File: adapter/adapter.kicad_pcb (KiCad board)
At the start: 2 copper layers, 93.5 x 50.9 mm, 41 parts, among them J10 Ribbon, J11 Ribbon, J12 Ribbon, J9 Ribbon, U1 nice_nano

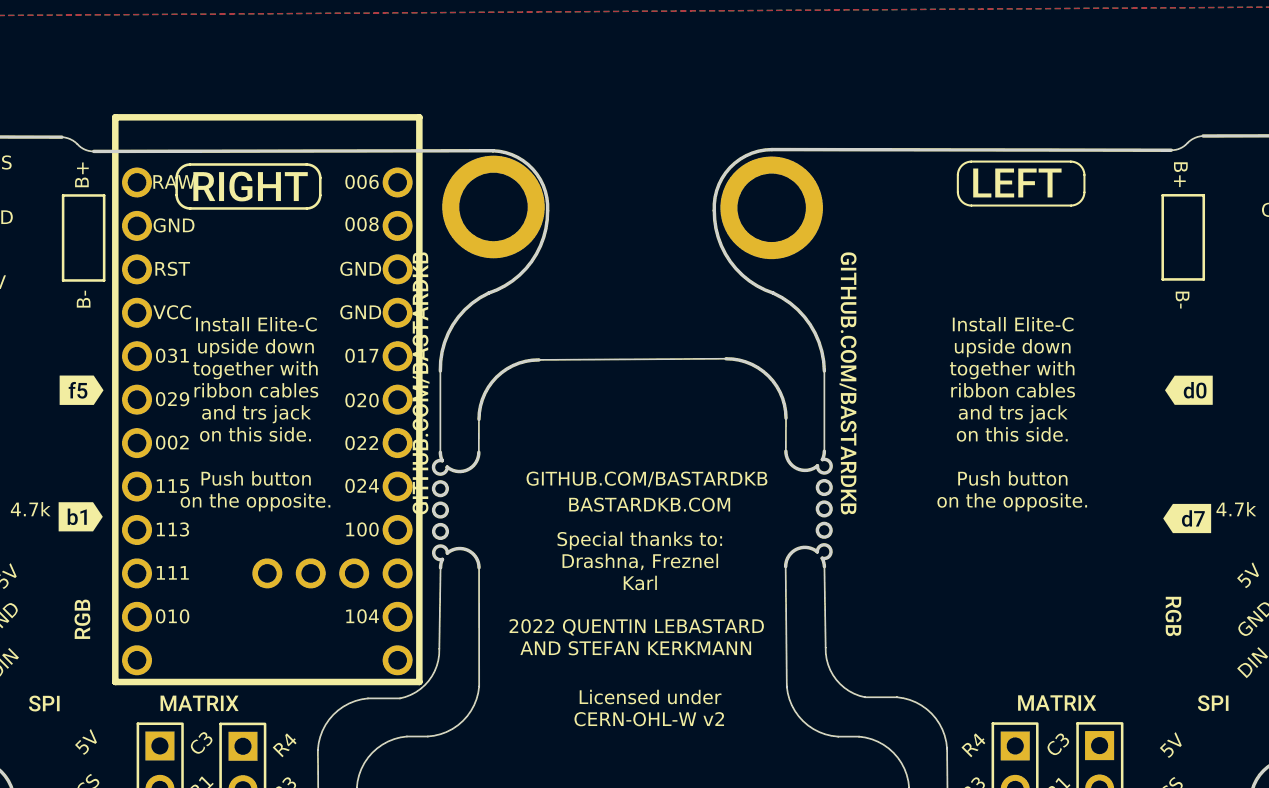
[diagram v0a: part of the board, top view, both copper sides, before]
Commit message: Add nice!nano mcu to right side
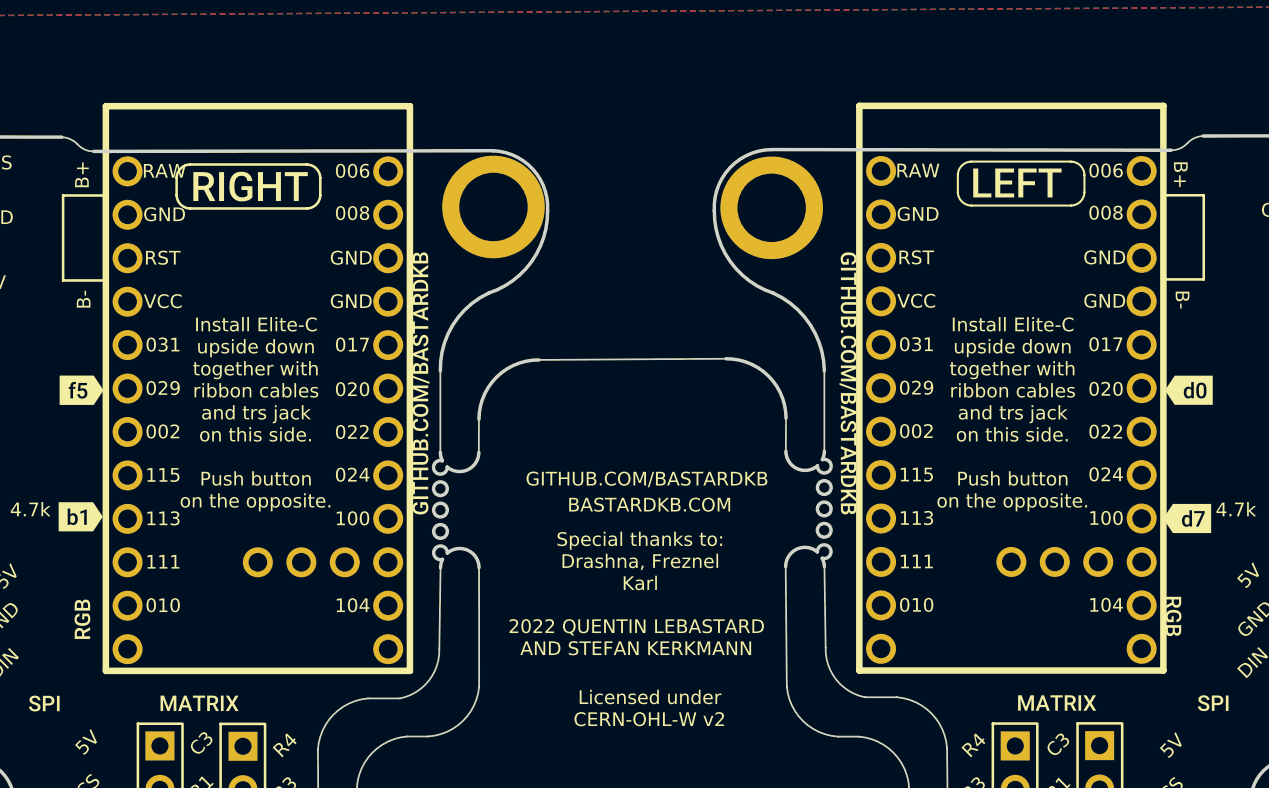
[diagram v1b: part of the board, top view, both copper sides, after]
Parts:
- added U2: nice_nano, Library:nice_nano, B.Cu at (177.6, 83.2)
- moved U1 0.85 mm to (133.6, 83.2)

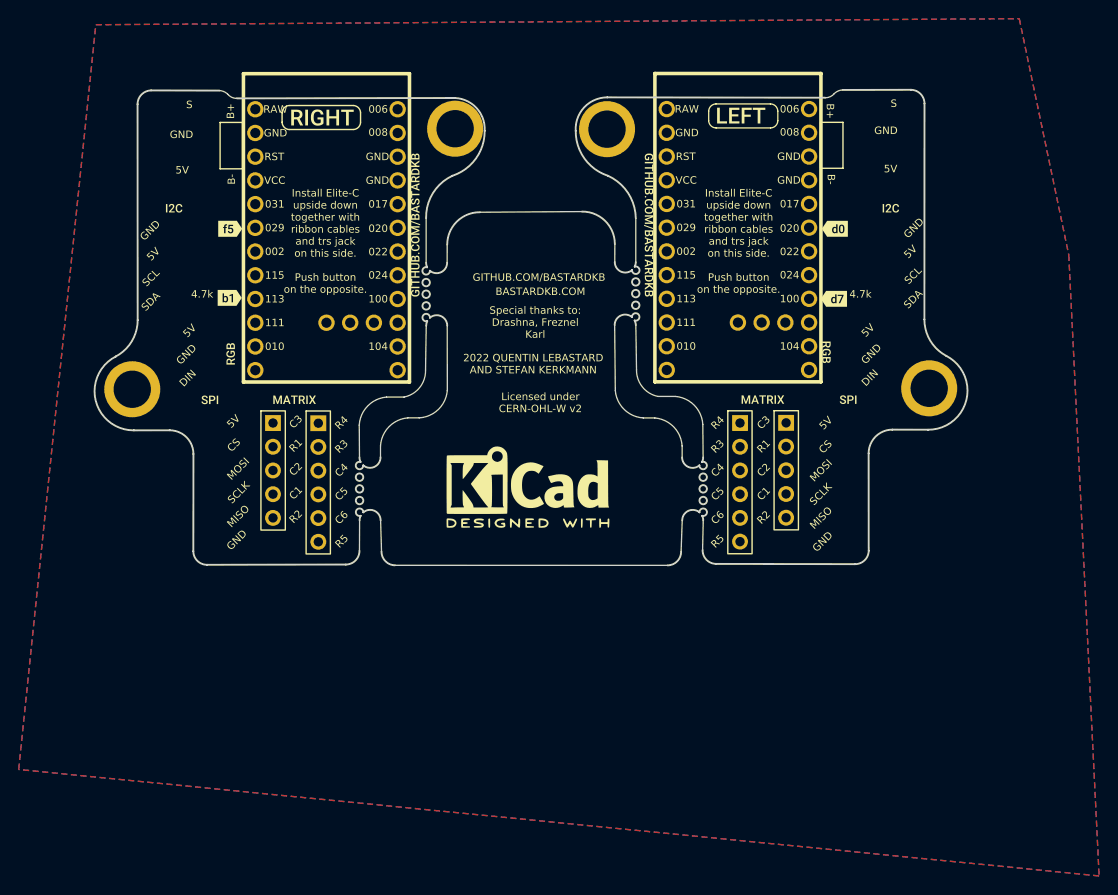
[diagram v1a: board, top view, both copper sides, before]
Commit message: Cleanup all the leftover silkscreen from removed parts
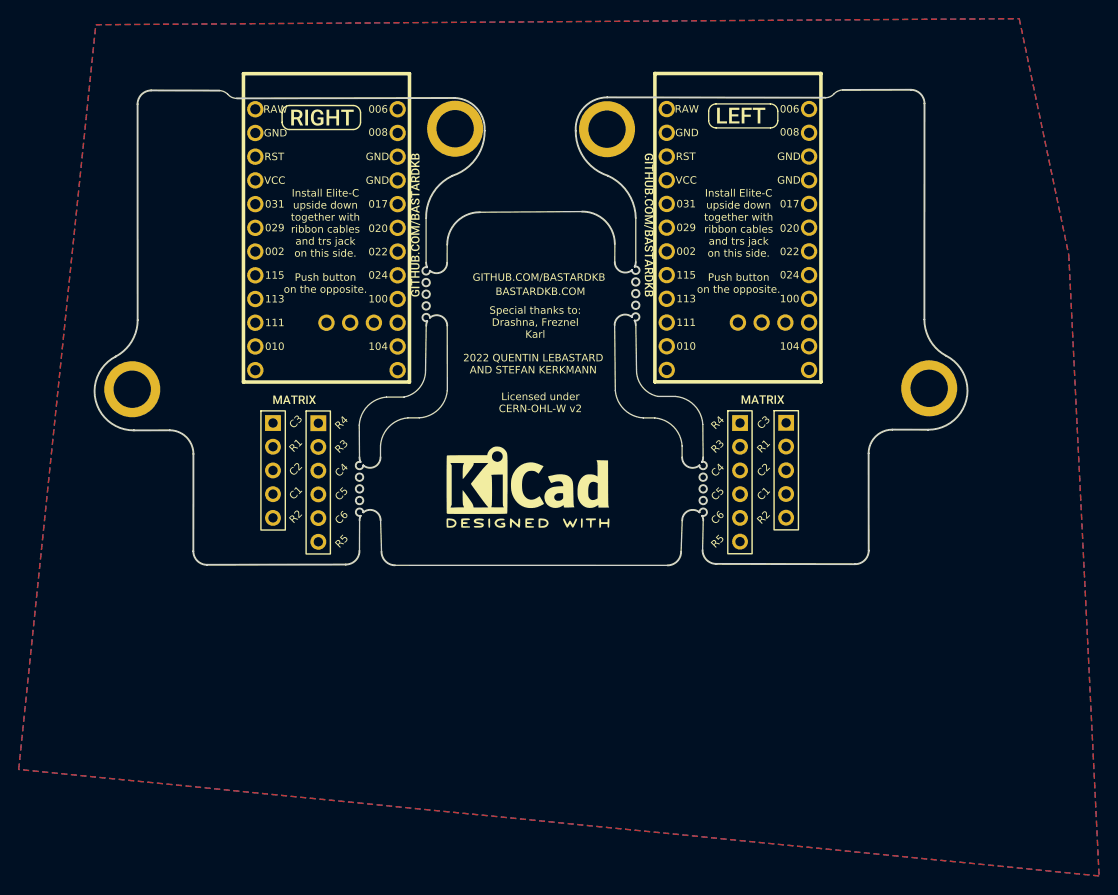
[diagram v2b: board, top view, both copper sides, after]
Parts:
- removed kibuzzard-61F01957 (x4): G***, kibuzzard-61F01957
- removed kibuzzard-61F019CB (x4): G***, kibuzzard-61F019CB
- removed kibuzzard-6208EDFE: G***, kibuzzard-6208EDFE
- removed kibuzzard-6208EE22: G***, kibuzzard-6208EE22
- removed kibuzzard-62093EDE: G***, kibuzzard-62093EDE
- removed kibuzzard-62094D1C: G***, kibuzzard-62094D1C
- removed the kibuzzard-620B8593 at (177.5, 78.6)
- removed kibuzzard-620B8D91 (x4): G***, kibuzzard-620B8D91
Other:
- board text removed: "4.7k"
- board text removed: "5V"
- board text removed: "B+"
- board text removed: "B-"
- board text removed: "CS"
- board text removed: "DIN"
- board text removed: "GND"
- board text removed: "MISO"
- board text removed: "MOSI"
- board text removed: "S"
- board text removed: "SCL"
- board text removed: "SCLK"
- board text removed: "SDA"

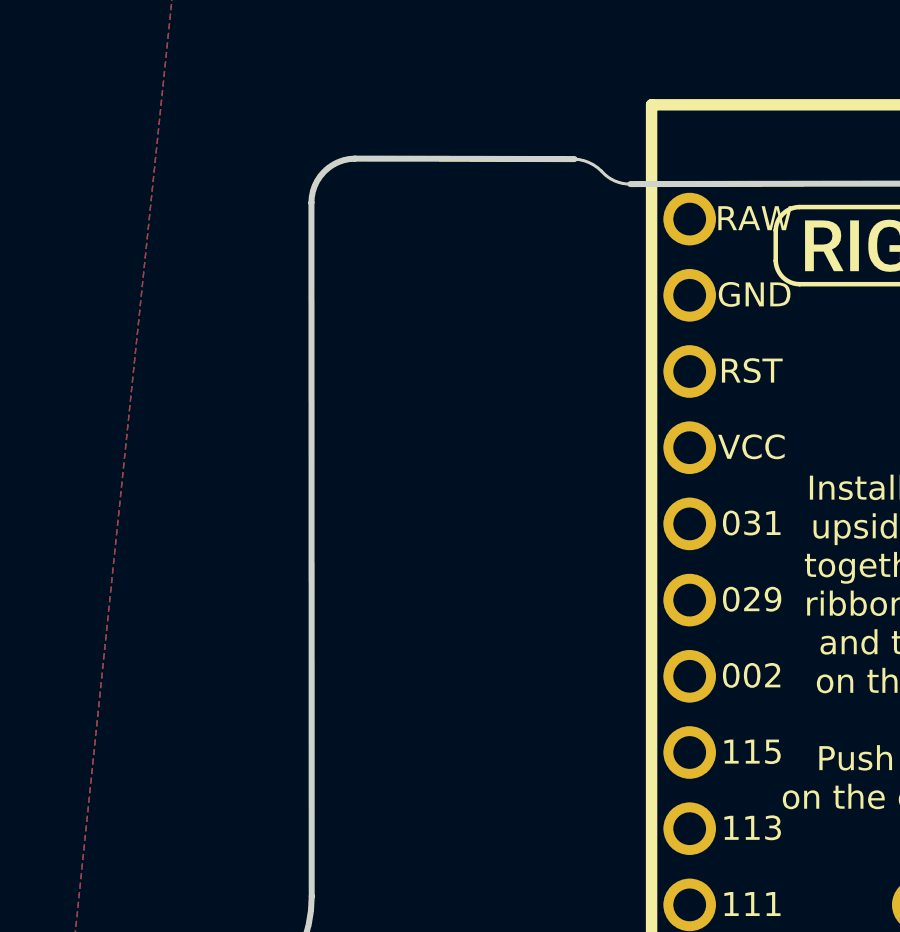
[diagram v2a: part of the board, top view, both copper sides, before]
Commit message: Add jst connector and powerswitch
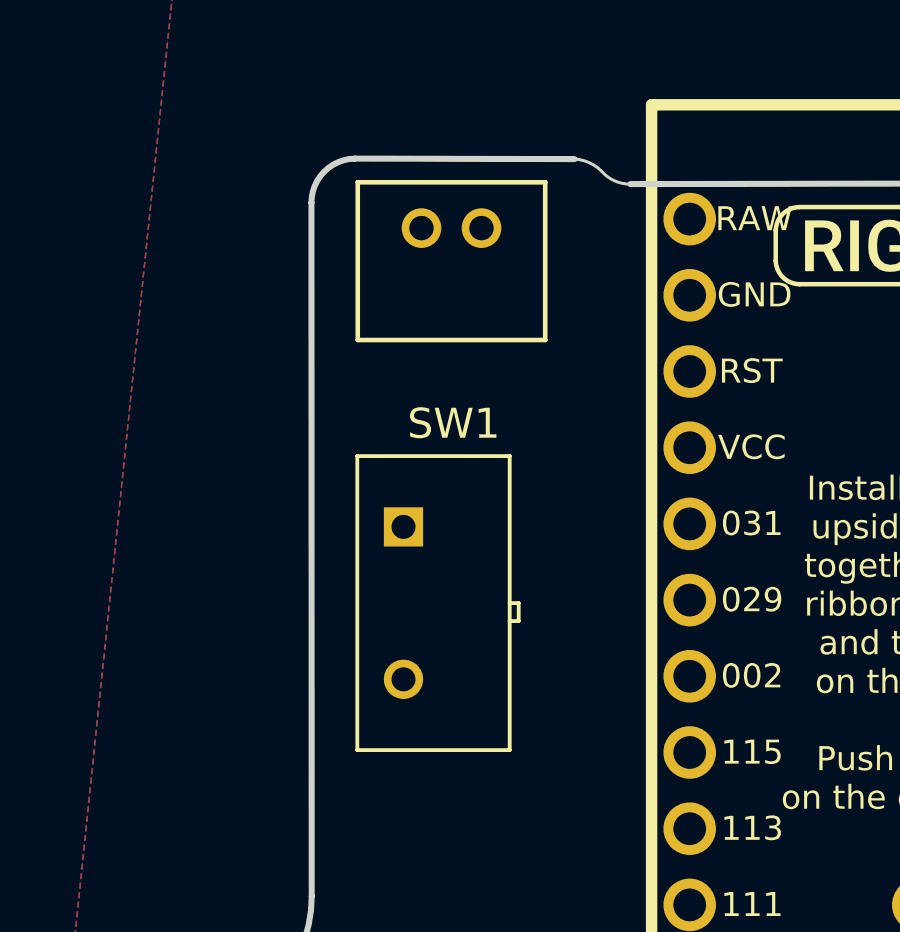
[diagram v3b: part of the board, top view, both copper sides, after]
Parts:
- added J1: DF3A-2P-2DSA, Library:DF3A_2P_2DSA, F.Cu at (117.0, 69.5)
- added SW1: AS11CP, Library:SW_AS11CP, F.Cu at (117.4, 82.0)
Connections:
- U1 pad 23: unconnected-(U1-GND-Pad23) -> GND
- U1 pad 24: unconnected-(U1-BATIN/P0.04-Pad24) -> BAT+

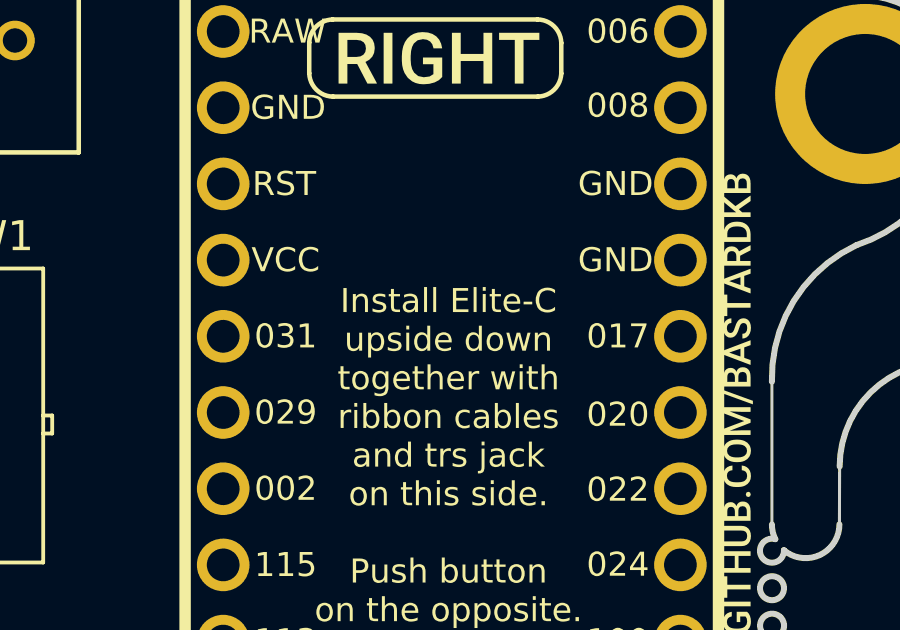
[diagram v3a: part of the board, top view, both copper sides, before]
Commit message: Add a resetbutton
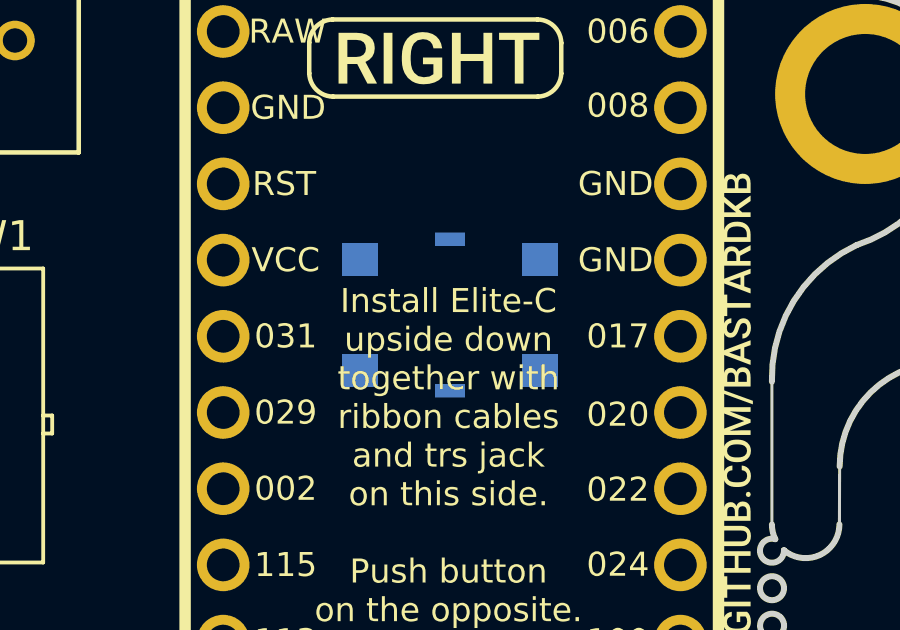
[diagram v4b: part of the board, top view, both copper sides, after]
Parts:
- removed kibuzzard-620B8593: G***, kibuzzard-620B8593
- added S1: 431151015826, Library:431151015826, B.Cu at (133.5, 78.7)
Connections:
- J1 pad 1: BAT+ -> GND
- J1 pad 2: GND -> BAT+
- U1 pad 22: unconnected-(U1-RST-Pad22) -> RST

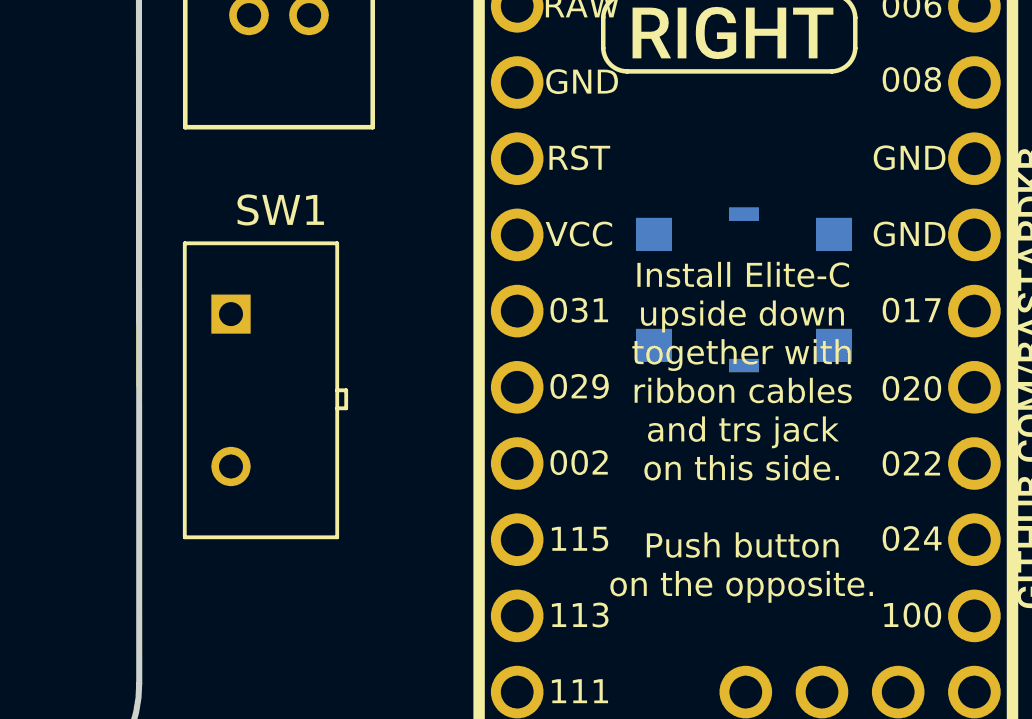
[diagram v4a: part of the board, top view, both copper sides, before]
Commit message: Remove power switch
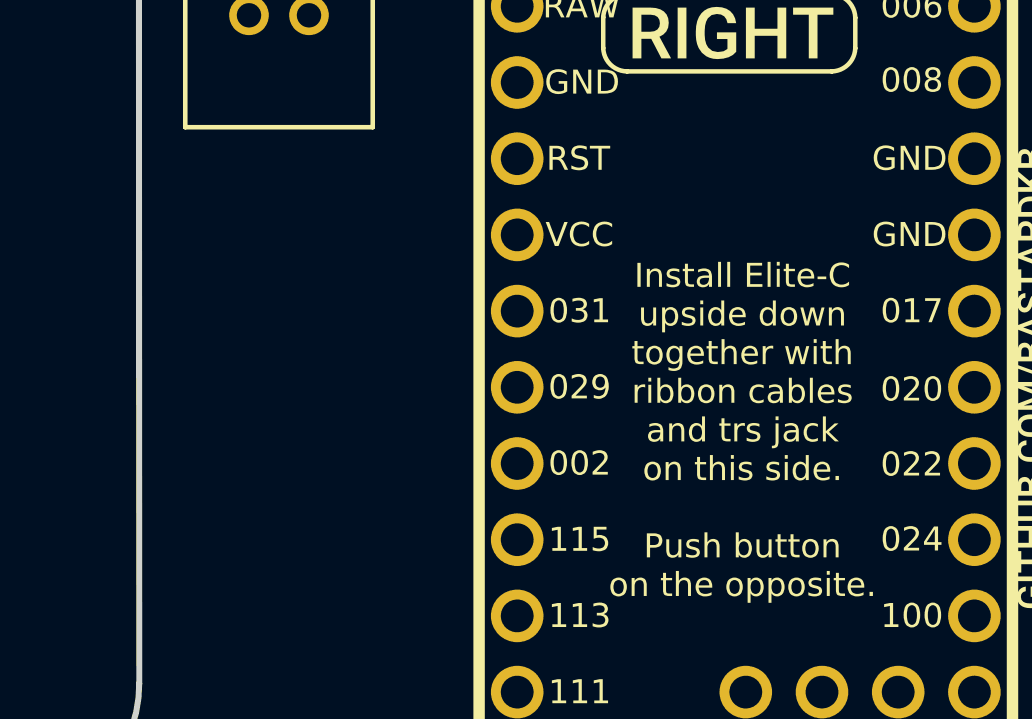
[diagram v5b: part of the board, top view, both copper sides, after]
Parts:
- removed S1: 431151015826, Library:431151015826
- removed SW1: AS11CP, Library:SW_AS11CP

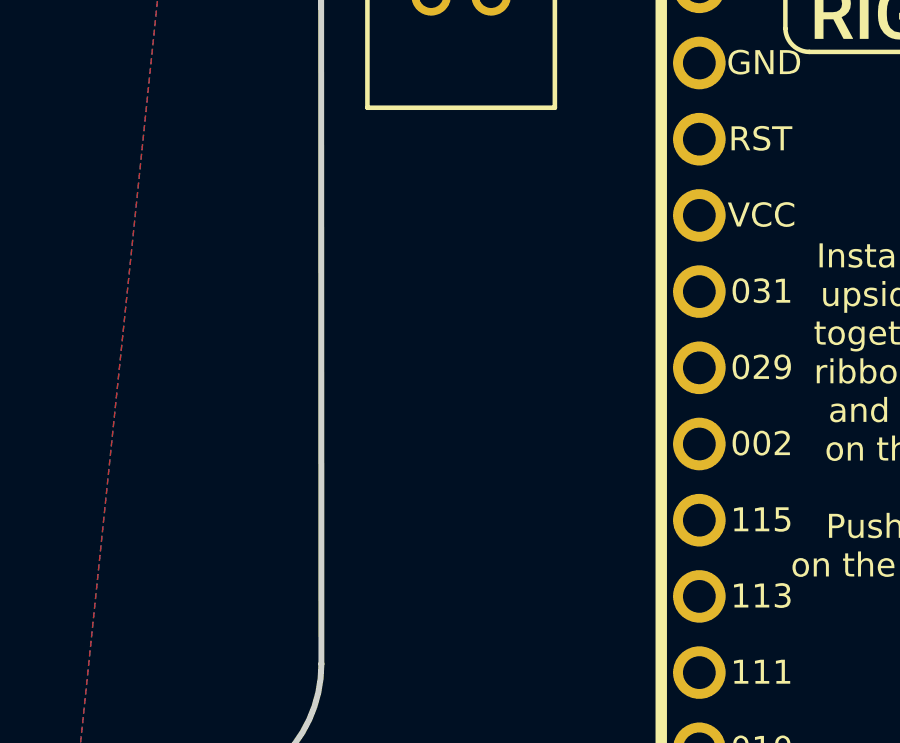
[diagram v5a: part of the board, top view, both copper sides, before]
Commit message: Add new power switch and reset button
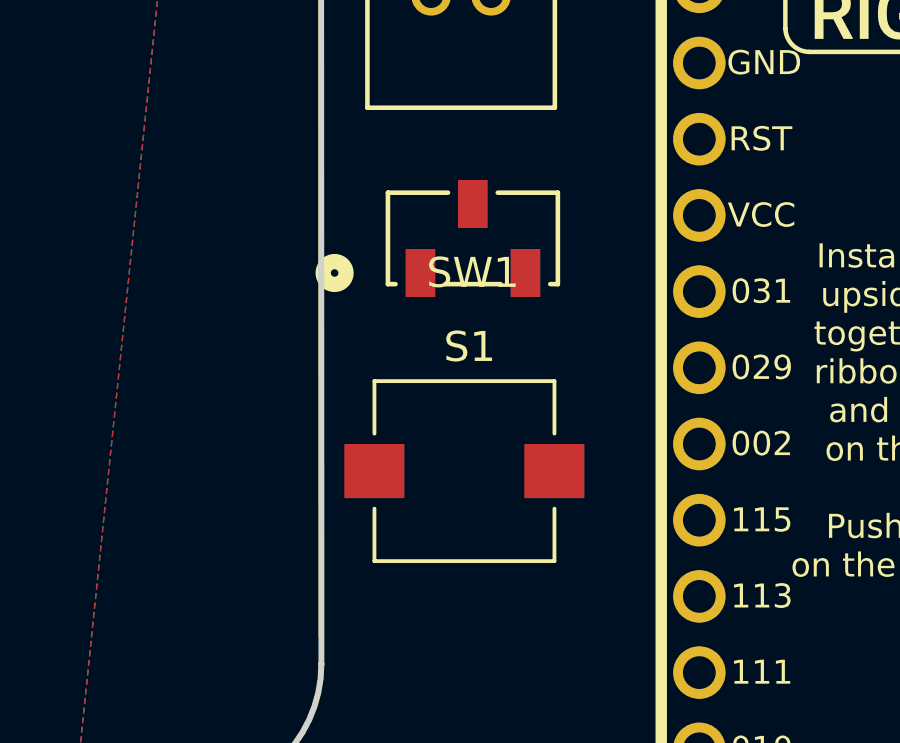
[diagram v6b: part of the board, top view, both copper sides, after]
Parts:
- added S1: TL9210AF180Q, Library:SW_TL9210AF180Q, F.Cu at (118.1, 85.3)
- added SW1: CAS-120TA, Library:CAS-120A_NDC, F.Cu at (118.4, 77.6)
